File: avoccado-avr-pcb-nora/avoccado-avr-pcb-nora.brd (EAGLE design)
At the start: 50 x 50 mm, 49 parts, among them Q1 16MHz, Q2 FET, U2 MCP73831

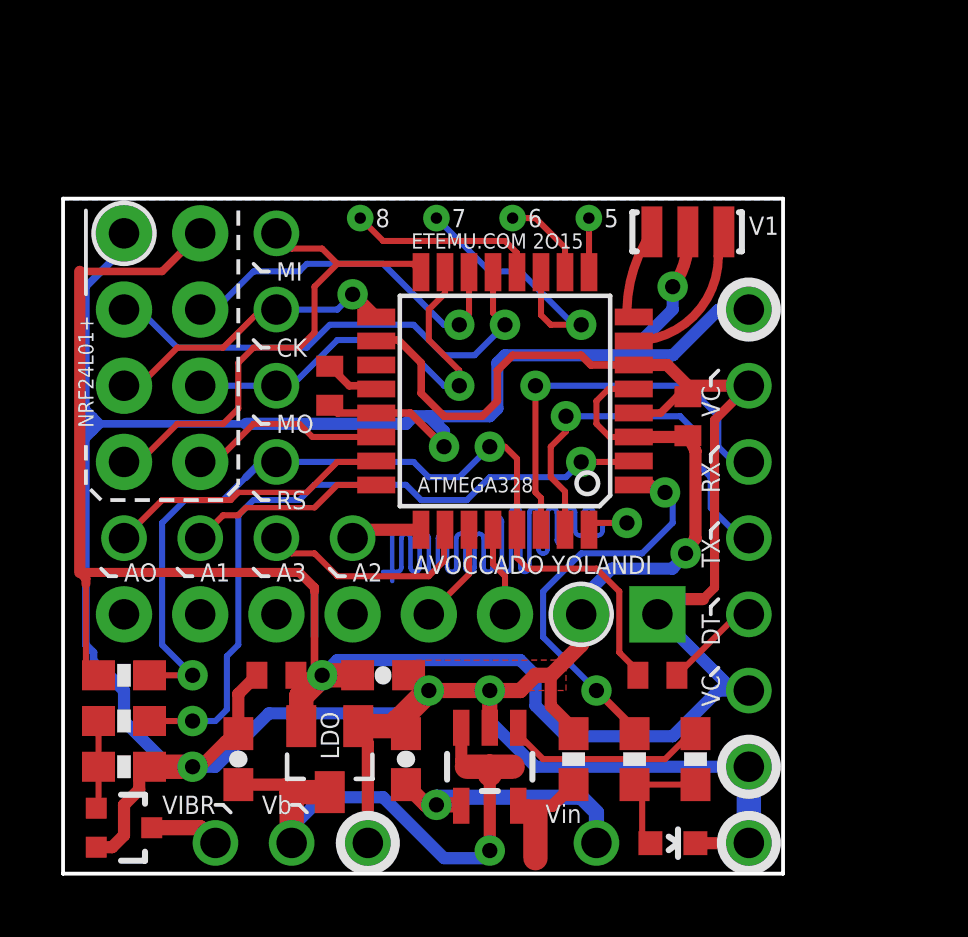
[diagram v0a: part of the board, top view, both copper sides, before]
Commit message: Nora: new PCB with plated half holes for surface mounting
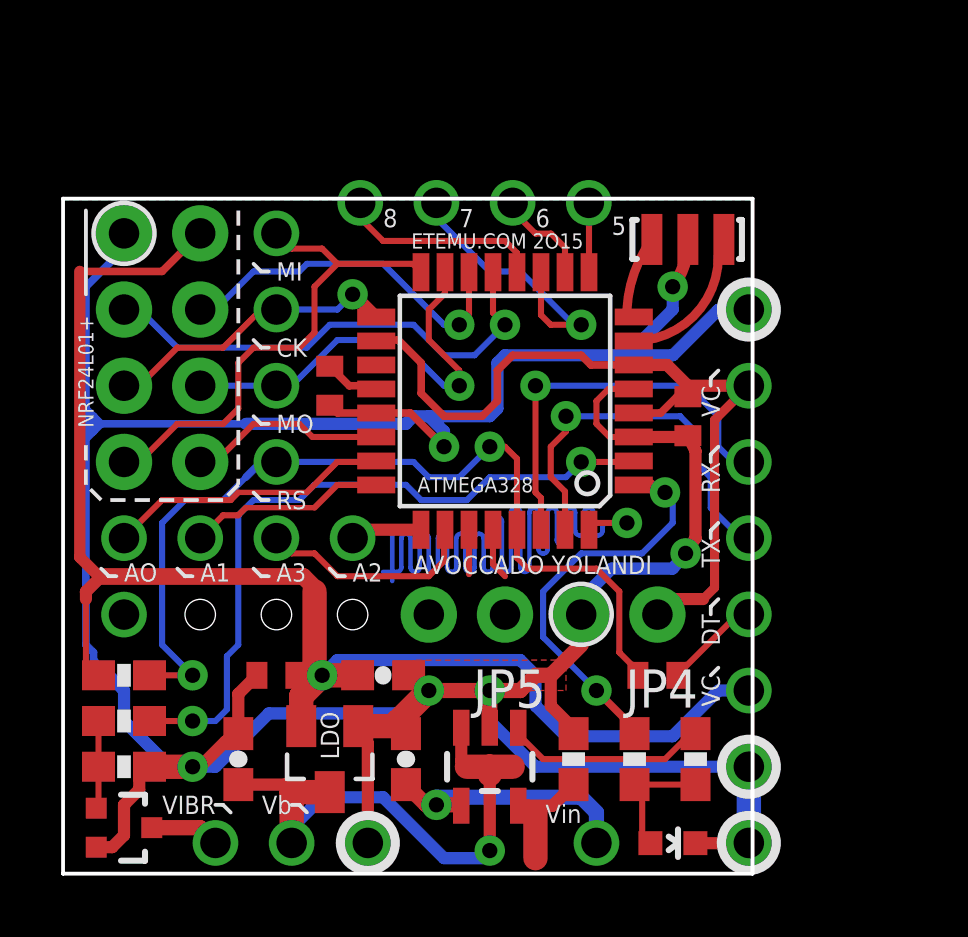
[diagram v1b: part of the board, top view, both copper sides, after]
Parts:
- removed JP1: MPU6050, SparkFun-Connectors:1X08_PIN1_NO_SILK
- added JP4, JP5: M021X02_NO_SILK, SparkFun-Connectors:1X02_NO_SILK
- added TP2: M01NOSILK-KIT, SparkFun-Connectors:1X01NS-KIT
- TP1, TP6, TP7, TP8: value TEST-POINTTP_15TH_THRU -> M01NOSILK-KIT; device SparkFun-Passives:TP_15TH -> SparkFun-Connectors:1X01NS-KIT
- moved TP1 0.51 mm to (17.5, 22.4)
- moved TP6 0.51 mm to (15.0, 22.4)
- moved TP7 0.51 mm to (12.4, 22.4)
- moved TP8 0.51 mm to (9.91, 22.4)
- moved Q1 0.25 mm to (20.8, 21.1)
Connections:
- net 3.3V: now also JP4.1; no longer JP1.1
- net A4: now also JP5.2; no longer JP1.4
- net A5: now also JP5.1; no longer JP1.3
- net D5: now also TP1.1; no longer TP1.P$1
- net D6: now also TP6.1; no longer TP6.P$1
- net D7: now also TP7.1; no longer TP7.P$1
- net D8: now also TP8.1; no longer TP8.P$1
- net GND: now also JP4.2; no longer JP1.2
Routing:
- net 3.3V: track 82.1 -> 77.5 mm
- net A4: track 3.37 -> 1.48 mm
- net GND: track 126.3 -> 124.5 mm
- net A5: track 2.99 -> 1.72 mm
- net D8: track 6.35 -> 6.86 mm
- net D7: track 9.20 -> 9.71 mm
- net D5: track 1.81 -> 2.31 mm
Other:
- outline, holes or cut-outs redrawn
- board text added: "WARNING DO NOT SWALLOW THIS PRODUCT"
- board text removed: "V1"
- board text removed: "WARNING - DO NOT SWALLOW THIS PRODUCT"
